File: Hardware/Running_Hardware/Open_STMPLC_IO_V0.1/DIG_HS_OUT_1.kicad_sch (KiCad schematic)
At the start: 25 parts, among them J1 Screw_Terminal_01x02, Q1 SUD50P06, Q2 AO3400A, U7 TPS26600PWP, U8 UCC23513

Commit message: Digital IO completion
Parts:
- removed Q1: SUD50P06, Package_TO_SOT_SMD:TO-252-3_TabPin2, symbol Transistor_FET:Q_PMOS_GDS
- removed Q2: AO3400A, Package_TO_SOT_SMD:SOT-23, symbol Transistor_FET:AO3400A
- removed R12, R13: 150R, Resistor_SMD:R_0603_1608Metric_Pad0.98x0.95mm_HandSolder, symbol Device:R_Small
- removed U8: UCC23513, Package_SO:SSO-6_6.8x4.6mm_P1.27mm_Clearance8mm, symbol UCC23153:UCC23513
- added D32, D33: SS510, Diode_SMD:D_SMA, symbol Device:D_Schottky_Small
- added Q2: 2N7002K, Package_TO_SOT_SMD:SOT-23, symbol Transistor_FET:2N7002K
- added U8: NVTFS5124PLTAG, NVTFS5124PLTAG:WDFN-8_3.3X3.3_P0.65mm, symbol MOSFET:NVTFS5124PLTAG
- D1: value SS54 -> SS510; footprint (none) -> Diode_SMD:D_SMA
- R1: value 10K -> 4.7K
- R2: value 47R -> 4.7K
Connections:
- net +24V: now also D33.2 (A); no longer C8.1, R5.2, U7.1 (IN), U7.2 (IN)
- net GND: now also D32.2 (A), Q2.2 (S)
- net at C1.1, C2.1, D4.1 (K)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: now also U8.1 (S), U8.2 (S), U8.3 (S)
- net at R11.2, R14.2: now also Q2.1 (G)
- net at D4.2 (A), R1.2, R2.1: now also U8.4 (G)
- net at R1.1: now also Q2.3 (D)
- net at D1.2 (A): now also D32.1 (K), U8.5, U8.6 (D), U8.7 (D), U8.8 (D)
- net HS_OUT_1 renamed DIG_HS_OUT_1
- net IMON renamed DIG_HS_IMON_1
- net ~{FAULT} renamed DIG_HS_~{FAULT}_1
- net ~{SHDN} renamed DIG_HS_~{SHDN}_1
- new net: C8.1, D33.1 (K), R5.2, U7.1 (IN), U7.2 (IN)
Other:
- moved on the sheet: C1, C2, C8, C9, D1, D3, D4, J1, R1, R11, R14, R2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

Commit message: Analog input section
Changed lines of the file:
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@@
 			(effects
 				(font
-					(size 1.27 1.27)
+					(size 1 1)
 				)
 				(justify left)
@@
 			(effects
 				(font
-					(size 1.27 1.27)
+					(size 1 1)
 				)
 				(justify left)
@@
 			(effects
 				(font
-					(size 1.27 1.27)
+					(size 1 1)
 				)
 				(justify left)
@@
 			(effects
 				(font
-					(size 1.27 1.27)
+					(size 1 1)
 				)
 				(justify left)

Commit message: GSM Module add
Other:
- title: (none) -> Open_PLC_IO
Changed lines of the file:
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@@
 	(generator_version "9.0")
 	(paper "A4")
+	(title_block
+		(title "Open_PLC_IO")
+		(date "2026-04-01")
+		(rev "0.1")
+	)
 	(rectangle
 		(start 13.97 13.97)

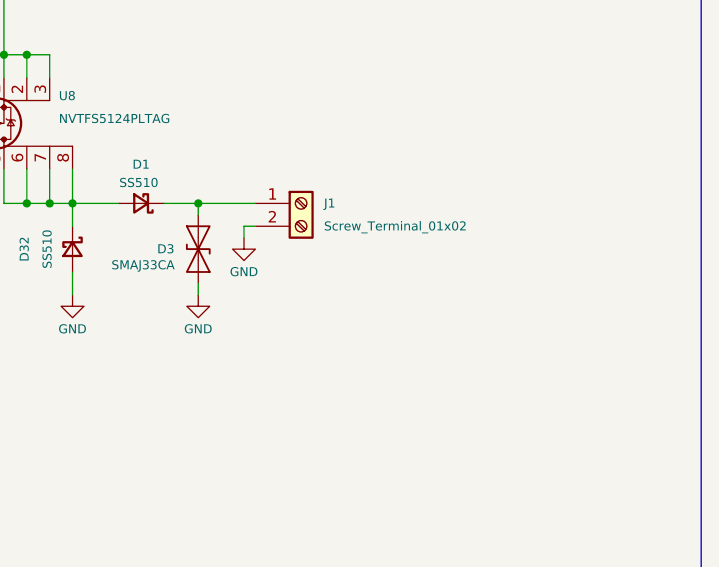
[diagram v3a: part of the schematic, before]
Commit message: Main PCB schematic changes V0.1
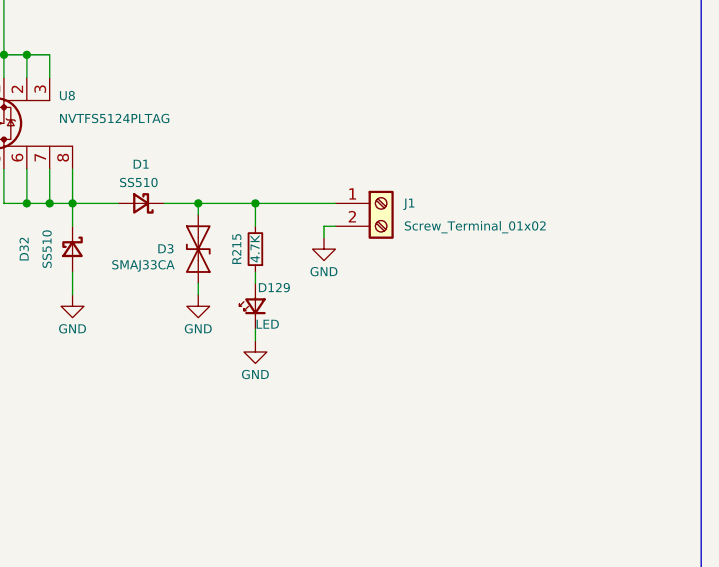
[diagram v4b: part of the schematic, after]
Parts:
- added D129: LED, LED_SMD:LED_0603_1608Metric_Pad1.05x0.95mm_HandSolder, symbol Device:LED_Small
- added R215: 4.7K, Resistor_SMD:R_0603_1608Metric_Pad0.98x0.95mm_HandSolder, symbol Device:R_Small
- C1, C8, C9: footprint (none) -> Capacitor_SMD:C_0603_1608Metric_Pad1.08x0.95mm_HandSolder
- C2: footprint (none) -> Capacitor_SMD:C_0805_2012Metric_Pad1.18x1.45mm_HandSolder
- D4: footprint (none) -> Diode_SMD:D_SOD-123
- J1: footprint (none) -> TerminalBlock_Phoenix:TerminalBlock_Phoenix_MKDS-1,5-2_1x02_P5.00mm_Horizontal
- R1, R11, R14, R2: footprint (none) -> Resistor_SMD:R_0603_1608Metric_Pad0.98x0.95mm_HandSolder
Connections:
- net GND: now also D129.1 (K)
- net at D1.1 (K), D3.1 (A1), J1.1 (Pin_1): now also R215.2
- new net: D129.2 (A), R215.1
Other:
- title: Open_PLC_IO -> Open_STMPLC_IO
- moved on the sheet: J1

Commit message: New DXF update
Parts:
- J1: footprint TerminalBlock_Phoenix:TerminalBlock_Phoenix_MKDS-1,5-2_1x02_P5.00mm_Horizontal -> TerminalBlock_Phoenix:TerminalBlock_Phoenix_MKDS-1-2-3.81_1x02_P3.81mm_Horizontal
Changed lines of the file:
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@@
 			)
 		)
-		(property "Footprint" "TerminalBlock_Phoenix:TerminalBlock_Phoenix_MKDS-1,5-2_1x02_P5.00mm_Horizontal"
+		(property "Footprint" "TerminalBlock_Phoenix:TerminalBlock_Phoenix_MKDS-1-2-3.81_1x02_P3.81mm_Horizontal"
 			(at 246.38 88.9 0)
 			(effects
@@
 		)
 		(instances
-			(project ""
+			(project "Open_STMPLC_IO_V0.1"
 				(path "/4d6787b6-1f4f-4098-b70b-d936e584350b/14439578-ba67-46a0-8d60-ec0dac961d93"
 					(reference "D129")

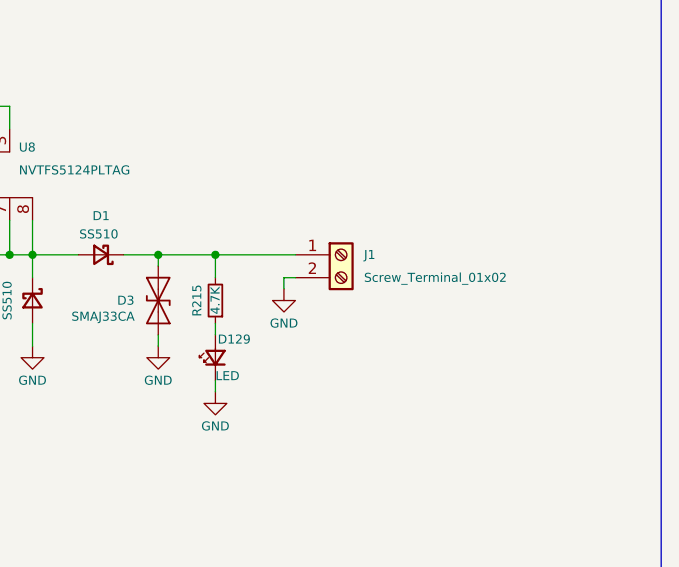
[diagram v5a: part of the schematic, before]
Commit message: Common GND terminal changes
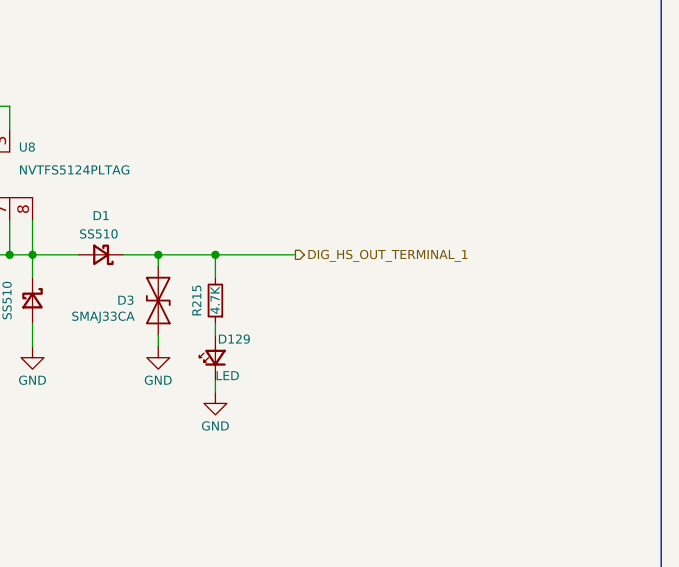
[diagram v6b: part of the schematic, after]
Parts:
- removed J1: Screw_Terminal_01x02, TerminalBlock_Phoenix:TerminalBlock_Phoenix_MKDS-1-2-3.81_1x02_P3.81mm_Horizontal, symbol Connector:Screw_Terminal_01x02
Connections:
- net DIG_HS_OUT_TERMINAL_1: now reaches D1.1 (K), D3.1 (A1), R215.2
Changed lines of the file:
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@@
-	(wire
-		(pts
-			(xy 240.03 92.71) (xy 240.03 91.44)
-		)
-		(stroke
-			(width 0)
-			(type default)
-		)
-	)
 	(wire
 		(pts
@@
 		(pts
 			(xy 212.09 88.9) (xy 209.55 88.9)
-		)
-		(stroke
-			(width 0)
-			(type default)
-		)
-	)
-	(wire
-		(pts
-			(xy 240.03 91.44) (xy 241.3 91.44)
 		)
 		(stroke
@@
 			)
 			(justify right)
+		)
+	)
+	(hierarchical_label "DIG_HS_OUT_TERMINAL_1"
+		(shape output)
+		(at 241.3 88.9 0)
+		(effects
+			(font
+				(size 1 1)
+			)
+			(justify left)
 		)
 	)
@@
 				(path "/4d6787b6-1f4f-4098-b70b-d936e584350b/14439578-ba67-46a0-8d60-ec0dac961d93"
 					(reference "#PWR017")
-					(unit 1)
-				)
-			)
-		)
-	)
-	(symbol
-		(lib_id "Connector:Screw_Terminal_01x02")
-		(at 246.38 88.9 0)
-		(unit 1)
-		(exclude_from_sim no)
-		(in_bom yes)
-		(on_board yes)
-		(dnp no)
-		(fields_autoplaced yes)
-		(property "Reference" "J1"
-			(at 248.92 88.8999 0)
-			(effects
-				(font
-					(size 1 1)
-				)
-				(justify left)
-			)
-		)
-		(property "Value" "Screw_Terminal_01x02"
-			(at 248.92 91.4399 0)
-			(effects
-				(font
-					(size 1 1)
-				)
-				(justify left)
-			)
-		)
-		(property "Footprint" "TerminalBlock_Phoenix:TerminalBlock_Phoenix_MKDS-1-2-3.81_1x02_P3.81mm_Horizontal"
-			(at 246.38 88.9 0)
-			(effects
-				(font
-					(size 1.27 1.27)
-				)
-				(hide yes)
-			)
-		)
-		(property "Datasheet" "~"
-			(at 246.38 88.9 0)
-			(effects
-				(font
-					(size 1.27 1.27)
-				)
-				(hide yes)
-			)
-		)
-		(property "Description" "Generic screw terminal, single row, 01x02, script generated (kicad-library-utils/schlib/autogen/connector/)"
-			(at 246.38 88.9 0)
-			(effects
-				(font
-					(size 1.27 1.27)
-				)
-				(hide yes)
-			)
-		)
-		(pin "1"
-		)
-		(pin "2"
-		)
-		(instances
-			(project "Open_STMPLC_IO_V0.1"
-				(path "/4d6787b6-1f4f-4098-b70b-d936e584350b/14439578-ba67-46a0-8d60-ec0dac961d93"
-					(reference "J1")
 					(unit 1)
 				)
@@
 					(unit 1)
 				)
-			)
-		)
-	)
-	(symbol
-		(lib_id "power:GND")
-		(at 240.03 92.71 0)
-		(unit 1)
-		(exclude_from_sim no)
-		(in_bom yes)
-		(on_board yes)
-		(dnp no)
-		(property "Reference" "#PWR05"
-			(at 240.03 99.06 0)
-			(effects
-				(font
-					(size 1 1)
-				)
-				(hide yes)
-			)
-		)
-		(property "Value" "GND"
-			(at 240.03 96.52 0)
-			(effects
-				(font
-					(size 1 1)
-				)
-			)
-		)
-		(property "Footprint" ""
-			(at 240.03 92.71 0)
-			(effects
-				(font
-					(size 1.27 1.27)
-				)
-				(hide yes)
-			)
-		)
-		(property "Datasheet" ""
-			(at 240.03 92.71 0)
-			(effects
-				(font
-					(size 1.27 1.27)
-				)
-				(hide yes)
-			)
-		)
-		(property "Description" "Power symbol creates a global label with name \"GND\" , ground"
-			(at 240.03 92.71 0)
-			(effects
-				(font
-					(size 1.27 1.27)
-				)
-				(hide yes)
-			)
-		)
-		(pin "1"
-		)
-		(instances
-			(project "Open_STMPLC_IO_V0.1"
-				(path "/4d6787b6-1f4f-4098-b70b-d936e584350b/14439578-ba67-46a0-8d60-ec0dac961d93"
-					(reference "#PWR05")
-					(unit 1)
-				)

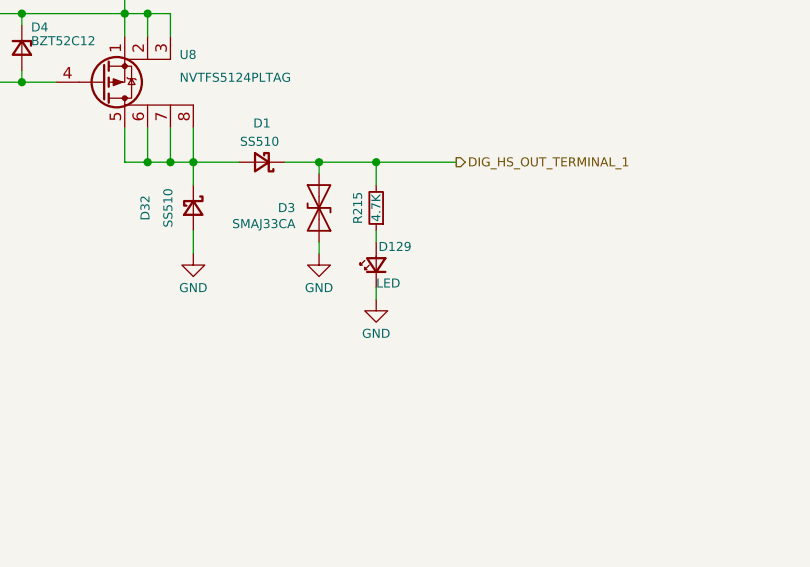
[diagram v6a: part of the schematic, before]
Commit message: Schematic updates
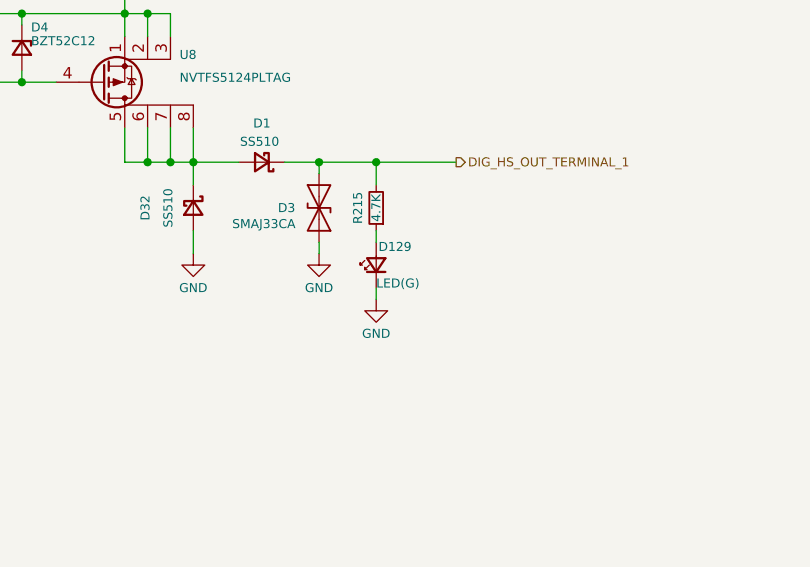
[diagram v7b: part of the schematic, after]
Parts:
- D129: value LED -> LED(G)
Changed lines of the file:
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@@
 			)
 		)
-		(property "Value" "LED"
+		(property "Value" "LED(G)"
 			(at 232.41 102.362 90)
 			(effects
